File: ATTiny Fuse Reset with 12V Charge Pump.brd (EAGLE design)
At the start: 45 parts, among them U2 ARDUINOR3-BPLACE

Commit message: Some cosmetic changes
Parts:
- C5: value 0.2uF -> 10uF
- ZD1: value 12V -> 12V_zener
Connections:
- net RESET renamed HV/RESET
- new net 12V: C4.1, D4.CQ, R6.2, R7.2, ZD1.C
- net N$14: no longer C4.1, D4.CQ, R6.2, R7.2, ZD1.C
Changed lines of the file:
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@@
 </element>
 <element name="JP12" library="microbuilder" package="2X05" value="" x="45.72" y="10.16" rot="R180"/>
-<element name="C5" library="ATtami" package="0805" value="0.2uF" x="-10.16" y="-5.08"/>
+<element name="C5" library="ATtami" package="0805" value="10uF" x="-10.16" y="-5.08"/>
 <element name="U$7" library="SparkFun-Electromechanical" package="KPS-1290" value="SWITCH_SPDT" x="-5.08" y="-12.7"/>
-<element name="ZD1" library="dp_devices" package="SOD-123" value="12V" x="-7.62" y="-20.32"/>
+<element name="ZD1" library="dp_devices" package="SOD-123" value="12V_zener" x="-7.62" y="-20.32"/>
 </elements>
 <signals>
@@
 </signal>
 <signal name="N$14">
-<contactref element="D4" pad="CQ"/>
-<contactref element="C4" pad="1"/>
-<contactref element="R6" pad="2"/>
-<contactref element="R7" pad="2"/>
 <contactref element="R4" pad="2"/>
 <contactref element="IC2" pad="2"/>
-<contactref element="ZD1" pad="C"/>
 <contactref element="IC1" pad="2"/>
-<wire x1="39.613" y1="43.434" x2="60.96" y2="44.069" width="0" layer="19" extent="1-1"/>
-<wire x1="35.56" y1="42.28" x2="39.613" y2="43.434" width="0" layer="19" extent="1-1"/>
-<wire x1="35.56" y1="40.27" x2="35.56" y2="42.28" width="0" layer="19" extent="1-1"/>
-<wire x1="31.75" y1="46.09" x2="35.56" y2="42.28" width="0" layer="19" extent="1-1"/>
-<wire x1="25.4" y1="35.56" x2="35.56" y2="40.27" width="0" layer="19" extent="1-1"/>
+<wire x1="25.4" y1="35.56" x2="31.75" y2="46.09" width="0" layer="19" extent="1-1"/>
 <wire x1="3.81" y1="38.1" x2="25.4" y2="35.56" width="0" layer="19" extent="1-1"/>
-<wire x1="-9.255" y1="-20.32" x2="3.81" y2="38.1" width="0" layer="19" extent="1-1"/>
 </signal>
 <signal name="P1">
@@
 <wire x1="55.88" y1="47.89" x2="55.88" y2="50.8" width="0" layer="19" extent="1-1"/>
 </signal>
-<signal name="RESET">
+<signal name="HV/RESET">
 <contactref element="T1" pad="2"/>
 <contactref element="R6" pad="1"/>
-<contactref element="JP12" pad="5"/>
-<contactref element="JP11" pad="5"/>
 <contactref element="IC2" pad="4"/>
 <contactref element="D5" pad="CQ"/>
 <contactref element="IC1" pad="1"/>
+<contactref element="JP11" pad="5"/>
+<contactref element="JP12" pad="5"/>
 <wire x1="41.413" y1="43.434" x2="44.77" y2="43.01" width="0" layer="19" extent="1-1"/>
 <wire x1="25.4" y1="33.02" x2="41.413" y2="43.434" width="0" layer="19" extent="1-1"/>
@@
 <wire x1="38.1" y1="2.54" x2="50.8" y2="8.89" width="0" layer="19" extent="1-1"/>
 </signal>
+<signal name="12V">
+<contactref element="R7" pad="2"/>
+<contactref element="ZD1" pad="C"/>
+<contactref element="D4" pad="CQ"/>
+<contactref element="R6" pad="2"/>
+<contactref element="C4" pad="1"/>
+<wire x1="39.613" y1="43.434" x2="60.96" y2="44.069" width="0" layer="19" extent="1-1"/>
+<wire x1="35.56" y1="42.28" x2="39.613" y2="43.434" width="0" layer="19" extent="1-1"/>
+<wire x1="35.56" y1="40.27" x2="35.56" y2="42.28" width="0" layer="19" extent="1-1"/>
+<wire x1="-9.255" y1="-20.32" x2="35.56" y2="40.27" width="0" layer="19" extent="1-1"/>
+</signal>
 </signals>

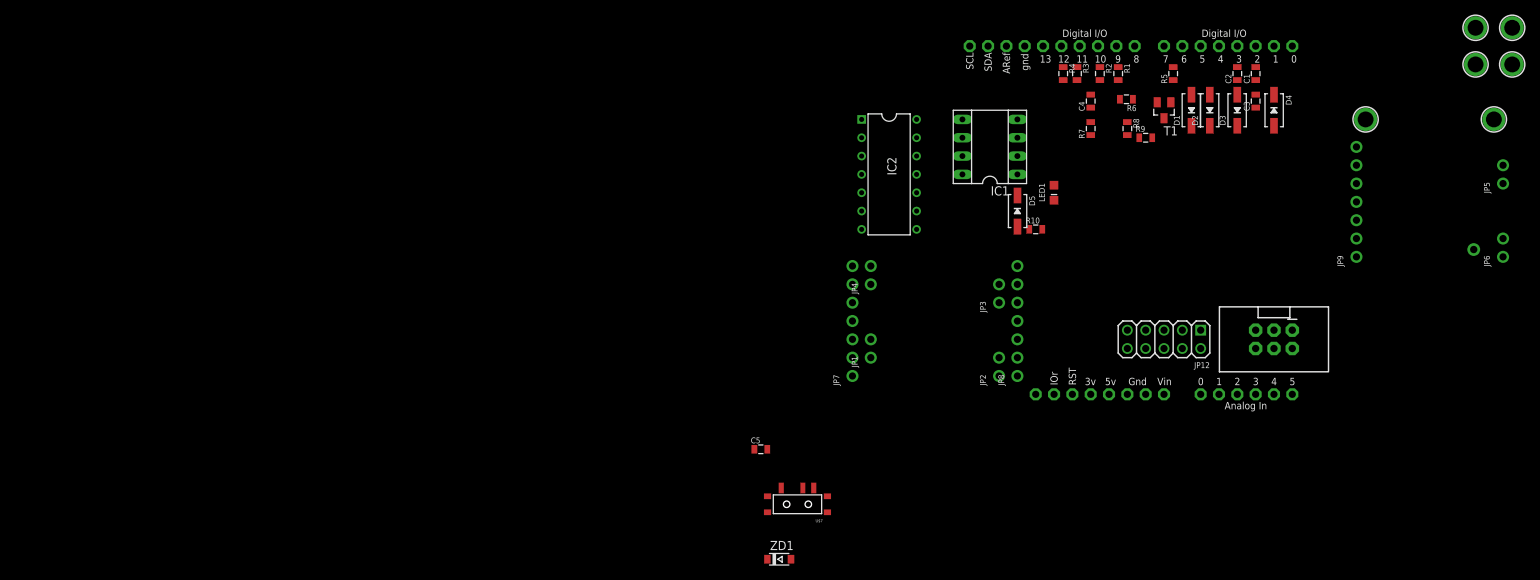
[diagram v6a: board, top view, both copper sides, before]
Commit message: layout and package of attami added
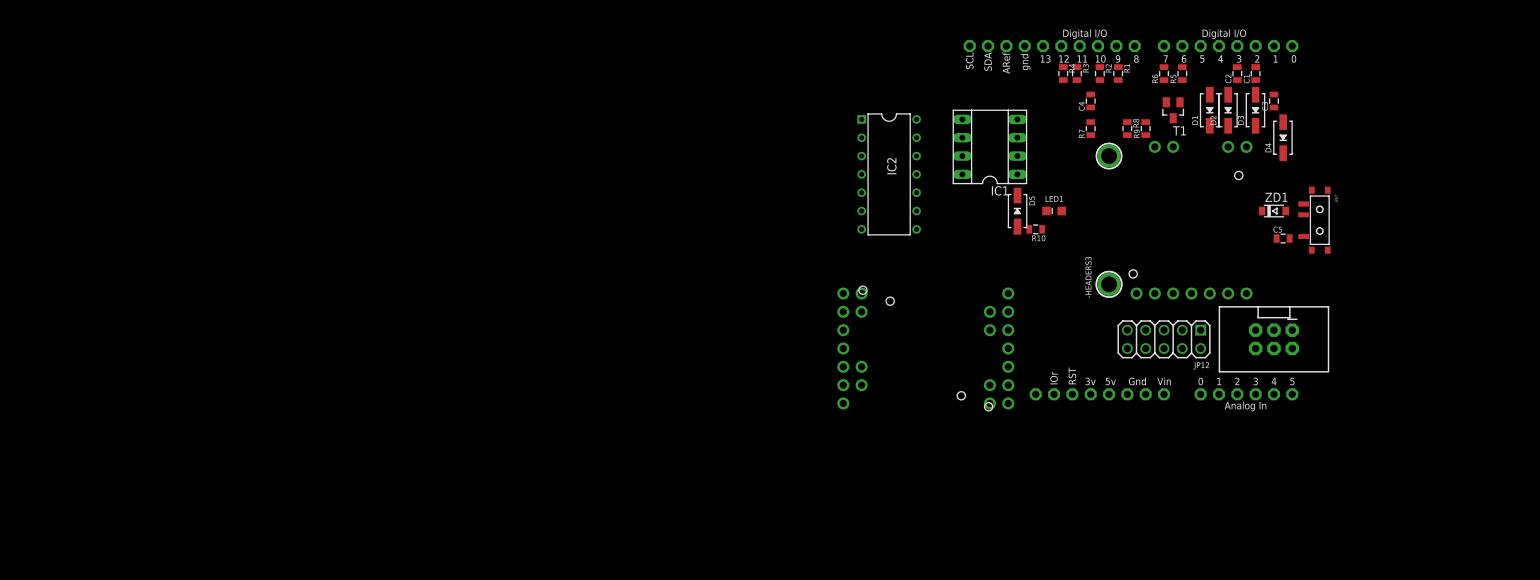
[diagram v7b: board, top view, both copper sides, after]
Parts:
- removed JP1, JP2, JP3, JP4, JP5, JP6: (no value), ATtami:1X02_ROUND
- removed JP10: (no value), ATtami:1X01-CLEANBIG
- removed JP7, JP8, JP9: (no value), ATtami:1X07_ROUND
- removed U$1, U$2, U$3, U$4: MOUNTINGHOLE2.0, ATtami:MOUNTINGHOLE_2.0_PLATED
- added -HEADERS1, -HEADERS2: (no value), ATtami:BREAKOUT_ATTAMI_HEADERS-ONLY
- added -HEADERS3: (no value), ATtami:BREAKOUT_ATTAMI
- moved ZD1 83.9 mm to (61.0, 27.9)
- moved U$7 82.4 mm to (67.3, 26.7), turned to 90 degrees
- moved C5 78.1 mm to (62.2, 24.1)
- moved U$5 59.2 mm to (38.1, 17.8)
- moved U$6 53.8 mm to (38.1, 35.6)
- moved R6 6.31 mm to (45.7, 47.0), turned to 90 degrees
- moved D4 4.02 mm to (62.2, 38.1), turned to 90 degrees
- moved C3 2.54 mm to (61.0, 43.2)
- moved D1 2.54 mm to (52.1, 41.9)
- moved D2 2.54 mm to (54.6, 41.9)
- moved D3 2.54 mm to (58.4, 41.9)
- moved LED1 2.54 mm to (30.5, 27.9), turned to 270 degrees
- moved T1 1.27 mm to (47.0, 41.9)
- moved R5 1.27 mm to (48.3, 47.0)
- moved R9 1.27 mm to (43.2, 39.4), turned to 90 degrees
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
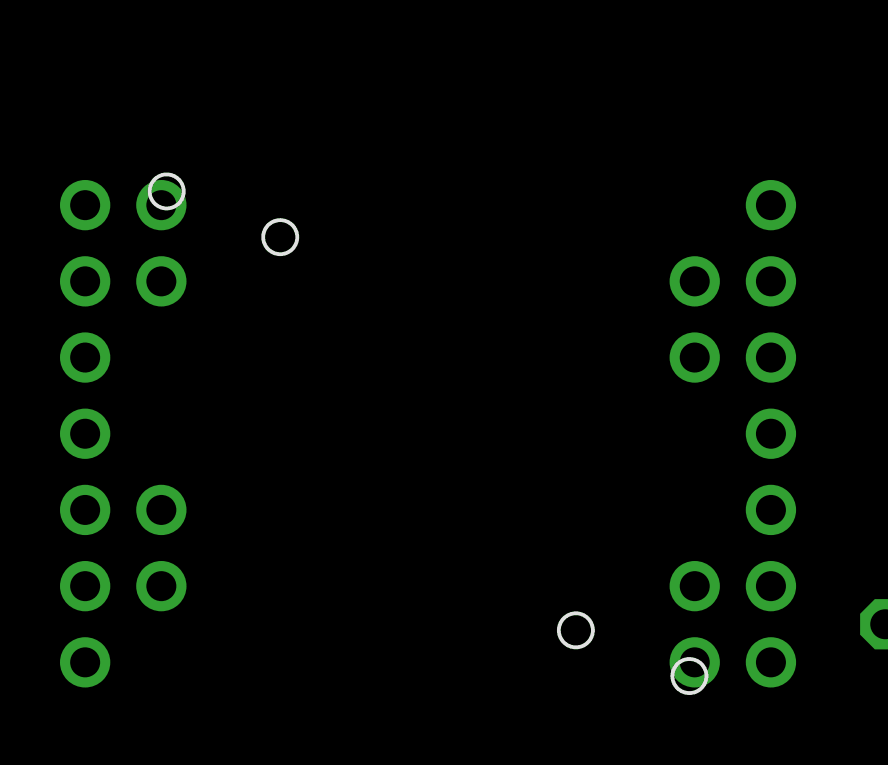
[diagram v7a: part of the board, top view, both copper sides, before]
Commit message: Mirroring one of the ATTami packages
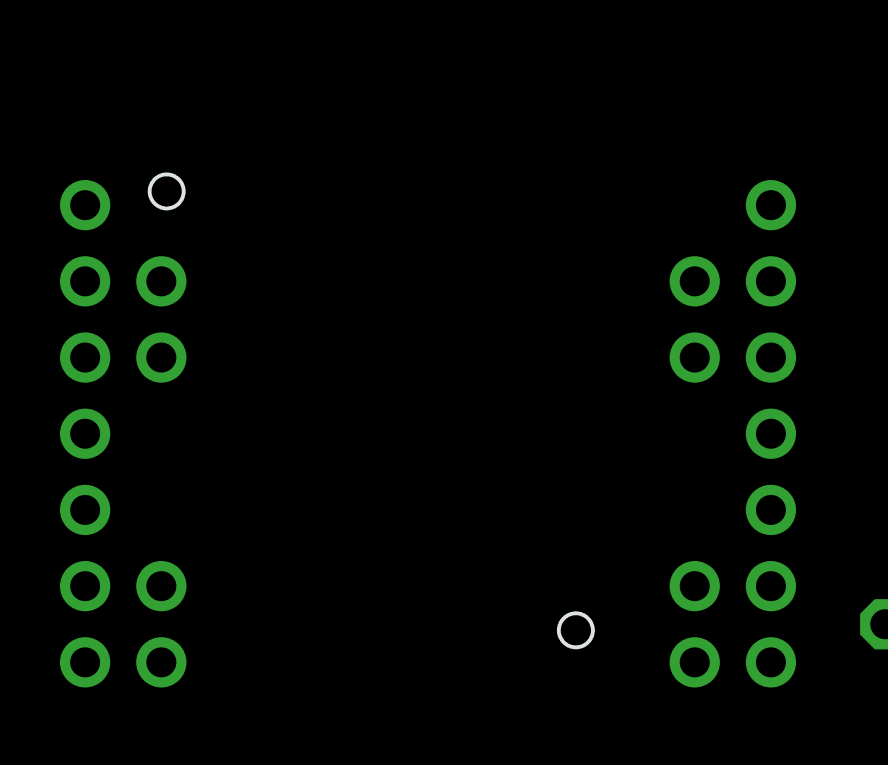
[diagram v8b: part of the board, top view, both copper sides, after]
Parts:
- moved -HEADERS2 17.8 mm to (25.4, 0.00), flipped to the bottom, turned to 0 degrees
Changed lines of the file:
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@@
 </element>
 <element name="-HEADERS1" library="ATtami" package="BREAKOUT_ATTAMI_HEADERS-ONLY" value="" x="0" y="0" smashed="yes"/>
-<element name="-HEADERS2" library="ATtami" package="BREAKOUT_ATTAMI_HEADERS-ONLY" value="" x="25.4" y="17.78" smashed="yes" rot="R180"/>
+<element name="-HEADERS2" library="ATtami" package="BREAKOUT_ATTAMI_HEADERS-ONLY" value="" x="25.4" y="0" smashed="yes" rot="MR0"/>
 <element name="-HEADERS3" library="ATtami" package="BREAKOUT_ATTAMI" value="" x="58.42" y="15.24" rot="R90"/>
 </elements>
